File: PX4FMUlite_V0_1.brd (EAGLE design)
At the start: 58.3 x 34.9 mm, 168 parts, among them J201 DF13C-6P-1.25V, J202 DF13C-6P-1.25V, J203 DF13C-6P-1.25V, J204 DF13C-6P-1.25V, J301 47346-0001, J302 DF13C-4P-1.25V, J401 DF13C-4P-1.25V, J403 DF13C-7P-1.25V, J404 DF13C-5P-1.25V, J405 DF13C-4P-1.25V, J601 DF13C-6P-1.25V, J702 DF13C-3P-1.25V, J801 JST-ZH-3, M3_MOUNT1101 MOUNT-HOLE3.1MM, M3_MOUNT1102 MOUNT-HOLE3.1MM, M3_MOUNT1103 MOUNT-HOLE3.1MM, M3_MOUNT1104 MOUNT-HOLE3.1MM, U101 STM32F4X7VX, U102 FM25V01, U301 2908-05WB-MG, U401 MAX3051, U502 L3GD20H, U701 TCA62724FMG, U703 LRTB GFTG-T7AW-1+V7A7-29+R5T9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, U903 74LVC2G240, X101 3.2x2.5 mm / 24 MHz / 15 ppm

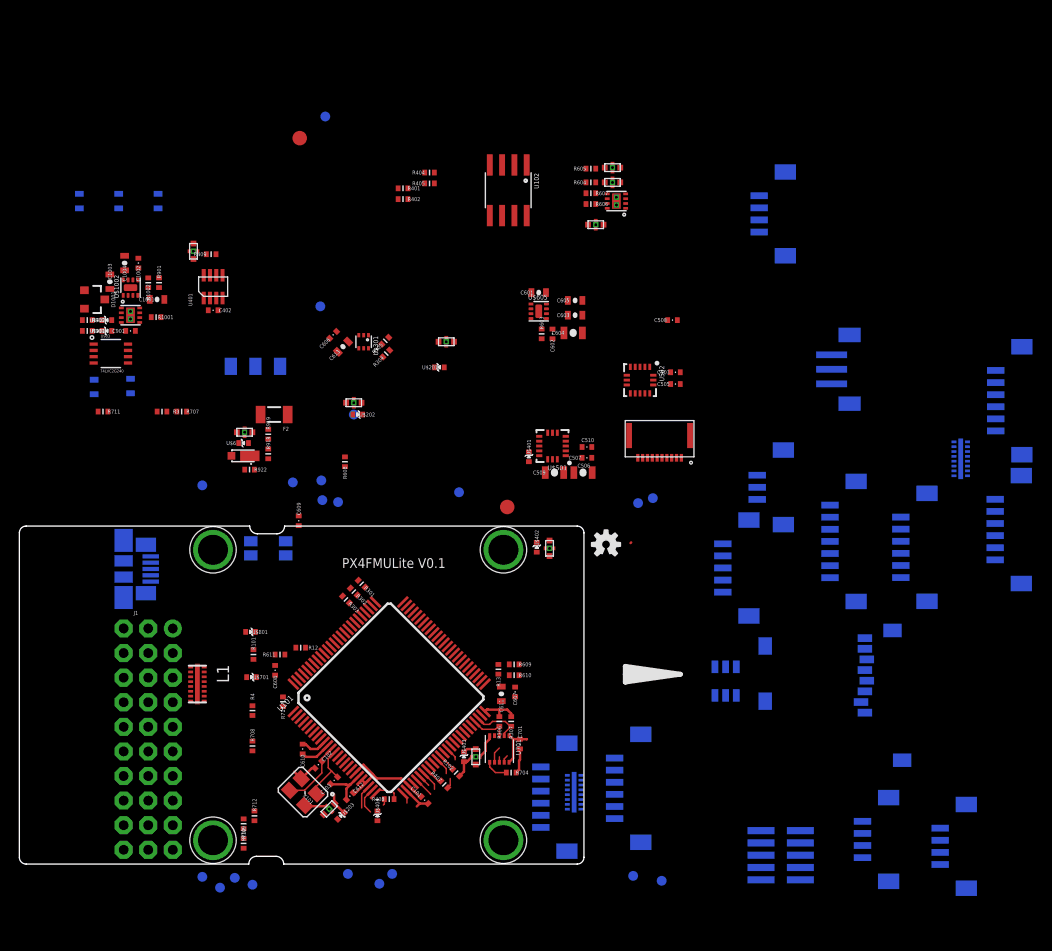
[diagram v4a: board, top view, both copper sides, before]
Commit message: Change to MPU6000 (sparkfun - needs changing),  Removed DF13 powerbrick conn
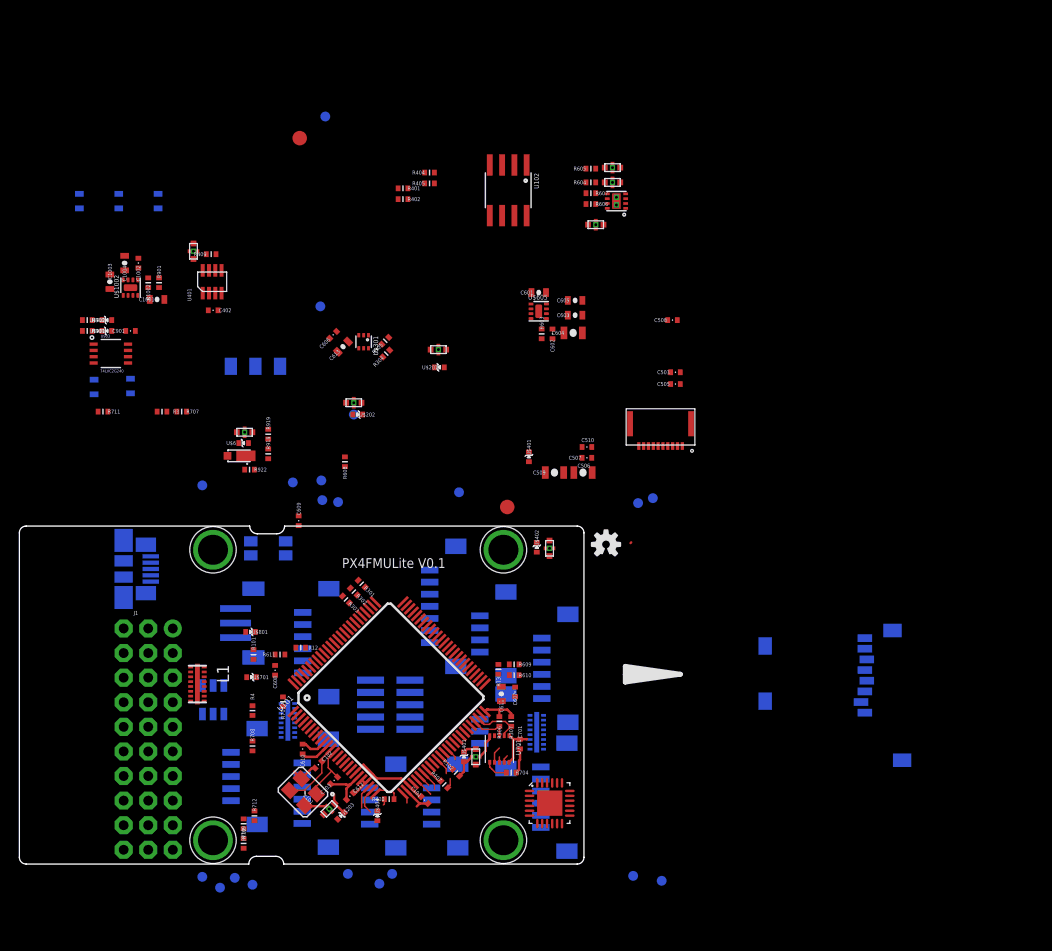
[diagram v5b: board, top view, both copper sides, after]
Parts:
- removed D1001: PMEG2005CT, pixhawk2:SOT23-3
- removed F2: 0ZCA0035FF2G, pixhawk2:PTC-1206
- removed J601: DF13C-6P-1.25V, con-hirose-df13:DF13C-6P-1.25V
- removed R1001: 100K, pixhawk2:0402-RES
- removed U$1001: BQ24313, pixhawk2:QFN8-DSG
- removed U$501: LSM303D, pixhawk2:LGA-16L
- removed U502: L3GD20H, pixhawk2:LGA-16L
- added U1: MPU-6000QFN-24, SparkFun-Sensors:QFN-24-TESTING
- moved J202 82.3 mm to (30.1, 10.1)
- moved L2 74.6 mm to (27.7, 17.6)
- moved J201 72.5 mm to (30.2, 25.6)
- moved J801 66.9 mm to (24.1, 27.6)
- moved J404 55.2 mm to (22.8, 11.8)
- moved U703 53.0 mm to (20.0, 19.7)
- moved J401 52.7 mm to (43.5, 8.74)
- moved J302 52.1 mm to (48.5, 26.5)
- moved J405 51.0 mm to (37.1, 8.74)
- moved JX301 43.2 mm to (38.3, 19.2)
- moved J403 41.9 mm to (43.3, 29.4)
- moved J702 38.2 mm to (48.5, 16.5)
- moved J203 14.5 mm to (54.9, 23.0)
- moved L3 7.30 mm to (53.4, 16.4)
- moved U$1 1.22 mm to (68.5, 45.9)
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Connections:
- net FMU-CH6 renamed FMU-CH8
- removed net BATT_CURRENT_SENS_PROT: J601.P$3, L601.P$1
- removed net IO-!VDD_SERVO_IN_FAULT: U$1001.4
- removed net IO-VDD_5V5: C1001.P$1, D1001.3, LED702.A, LED703.A, LED705.A, U$1002.1, U$1002.4
- removed net N$20: R1001.P$2, U$1001.7
- removed net N$4: D1001.2, U$1001.8
- removed net N$46: D1001.1, F2.2
- new net FMU-VDD_5V: C1001.P$1, LED702.A, LED703.A, LED705.A, U$1002.1, U$1002.4
- new net N$18: L1.P$8
- new net N$21: L601.P$1
- net !ACCEL_MAG_CS: no longer U$501.8
- net !GYRO_CS: no longer U502.5
- net ACCEL_DRDY: no longer U$501.11
- net BATT_VOLTAGE_SENS_PROT: no longer J601.P$4
- net GNDX: no longer J601.P$5, J601.P$6, R1001.P$1, U$1001.2, U$1001.5, U$1001.6, U$1001.GND, U$1001.P$2, U$1001.P$3, U$501.10, U$501.12, U$501.13, U$501.16, U$501.5, U502.10, U502.11, U502.12, U502.13, U502.9
- net GYRO_DRDY: no longer U502.6
- net MAG_DRDY: no longer U$501.9
- net N$10: no longer U$501.2
- net N$17: no longer U$501.3
- net N$30: no longer U502.14
- net N$6: no longer U$501.15
- net SPI_INT_MISO: no longer U$501.7, U502.4
- net SPI_INT_MOSI: no longer U$501.6, U502.3
- net SPI_INT_SCK: no longer U$501.4, U502.2
- net VDD_3V3_SENSORS: no longer U$501.1, U$501.14, U502.1, U502.15, U502.16
- net VDD_5V_BRICK: no longer J601.P$1, J601.P$2
- net VDD_5V_IN: no longer F2.1
- net VDD_SERVO_IN: no longer U$1001.1
